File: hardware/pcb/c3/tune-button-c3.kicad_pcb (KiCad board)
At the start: 2 copper layers, 46 x 70 mm, 42 parts, among them J1 USB-C, J2 LiPo, Q1 AO3401A, SW1 MX switch, SW2 MX switch, SW3 MX switch, SW4 MX switch, SW5 RESET, SW6 BOOT, U1 ESP32-C3-WROOM-02-N4, U2 SRV05-4, U3 TP4054, U4 RT9080-3.3

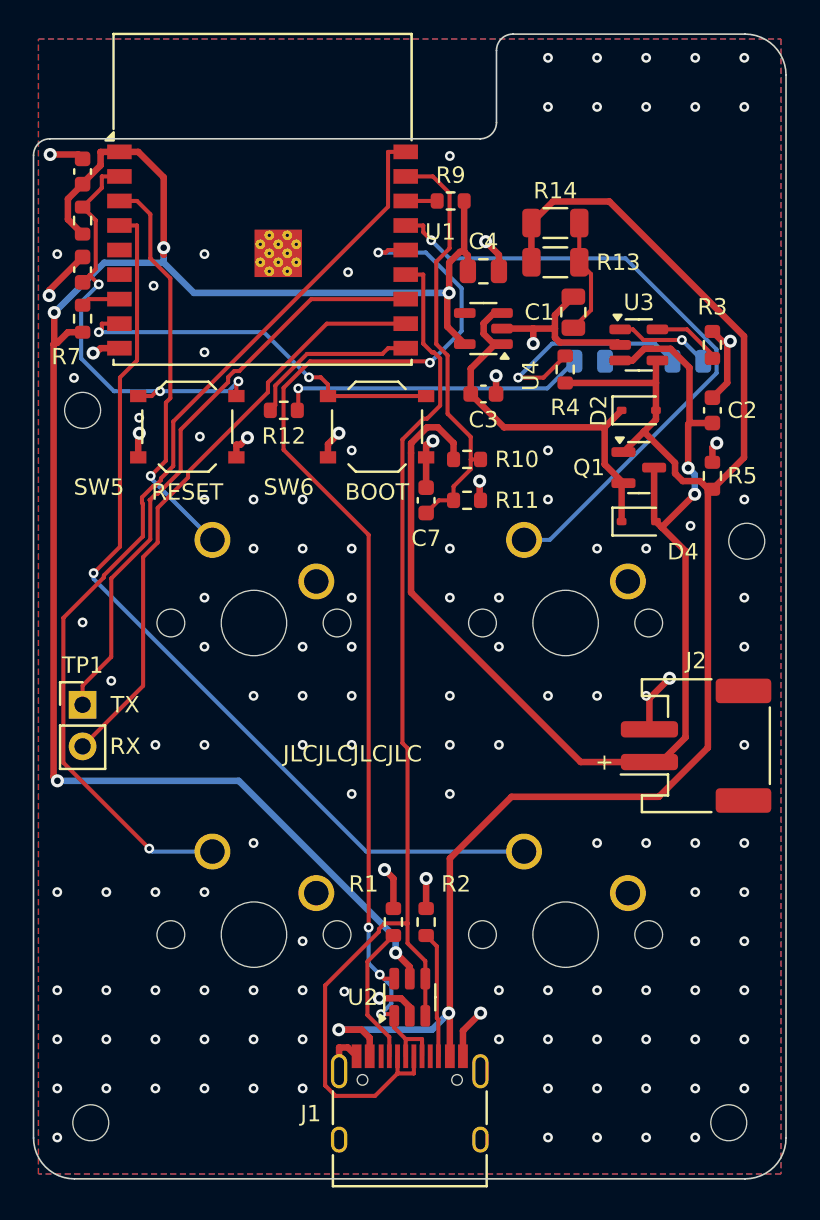
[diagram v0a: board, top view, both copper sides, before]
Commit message: pcb (c3): USB-C at HRO's recommended board edge
HRO's layout puts the board edge 5.79 mm from the receptacle's locating
holes, so its face overhangs by 0.46 mm. It was 6.05 mm (0.2 mm overhang),
which JLC's +-0.2 mm outline tolerance could take to flush, leaving a plug's
moulding nothing to clear the board by. The board is 0.26 mm shorter
(46 x 69.7 mm): the USB-C keeps its place relative to the keys, and what is
placed from the bottom edge (U2, R1, R2, the lower mounting holes) moves up
with it.
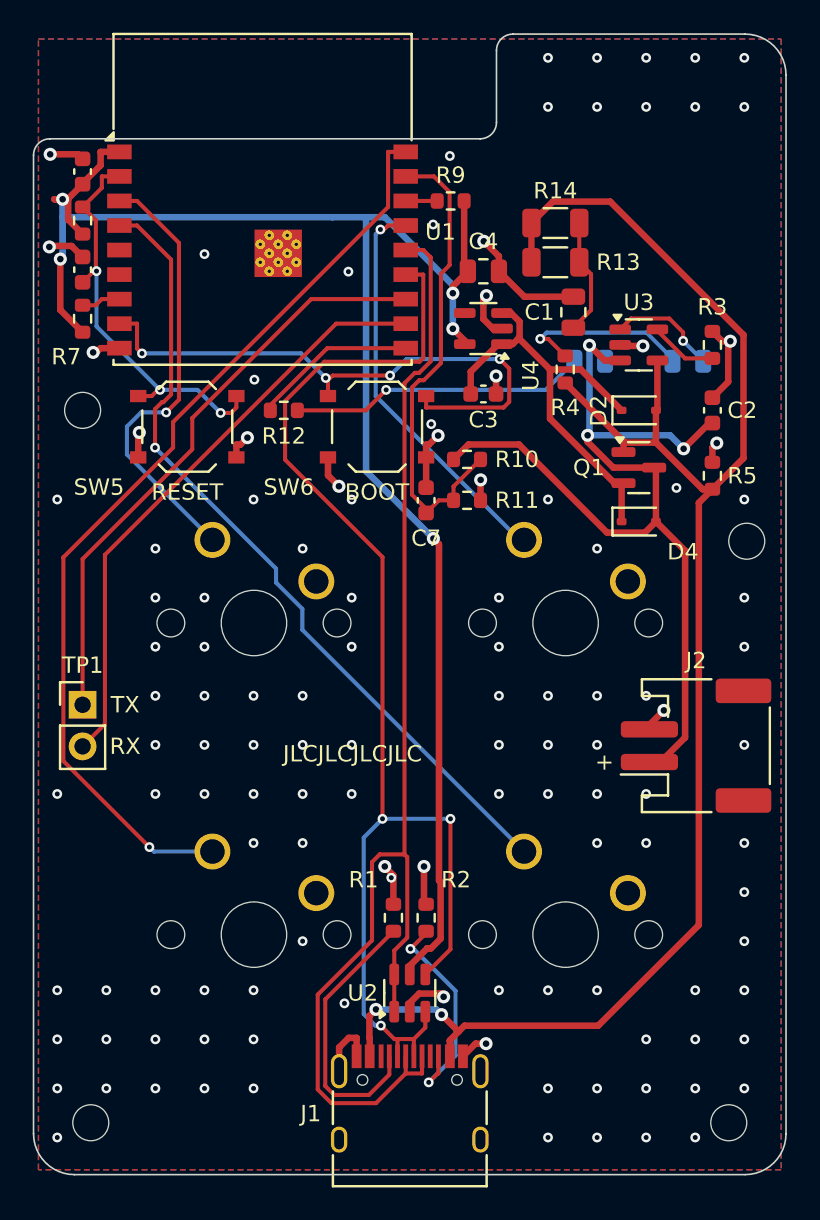
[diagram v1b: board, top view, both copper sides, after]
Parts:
- moved U2 0.26 mm to (23.0, 58.6)
- moved R1 0.26 mm to (22.0, 54.0)
- moved R2 0.26 mm to (24.0, 54.0)
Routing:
- net K1: track 39.8 -> 24.7 mm
- net VBAT: track 69.7 -> 57.2 mm, vias 2 -> 3
- net IO9: track 23.7 -> 35.9 mm, vias 2 -> 4
- net 3V3: track 112.7 -> 102.2 mm
- net USB_DN: track 69.7 -> 78.2 mm, vias 0 -> 3
- net CC1: track 8.59 -> 17.0 mm
- net K3: track 57.0 -> 50.0 mm
- net CC2: track 7.69 -> 13.4 mm, vias 0 -> 2
- net USB_DP: track 70.7 -> 76.1 mm, vias 5 -> 0
- net VSYS: track 23.8 -> 27.1 mm
- net GND: track 54.4 -> 51.1 mm, vias 134 -> 124
- net VBAT_SENSE: track 26.1 -> 29.3 mm
- net CHG_A: track 14.2 -> 11.0 mm
- net VBUS: track 104.5 -> 101.6 mm
- net K2: track 24.7 -> 27.2 mm
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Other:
- board size 46 x 70 mm -> 46 x 69.7 mm

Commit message: pcb: fixes from the sixth DFM audit
- Back-side SMD parts (the hand-soldered LEDs) get a rule area between
  their pads: no tracks, vias or pour there. The re-route had threaded
  VBAT between D3's pads, beside its GND pad, where a solder bridge would
  short the battery.
- Stitching now aims for two GND vias at least 2 mm apart in every pour
  island, not one. U3's ground pad (the charger's heat path) sits on a
  30 mm2 island with three vias; it had been on a 10 mm2 one with one.
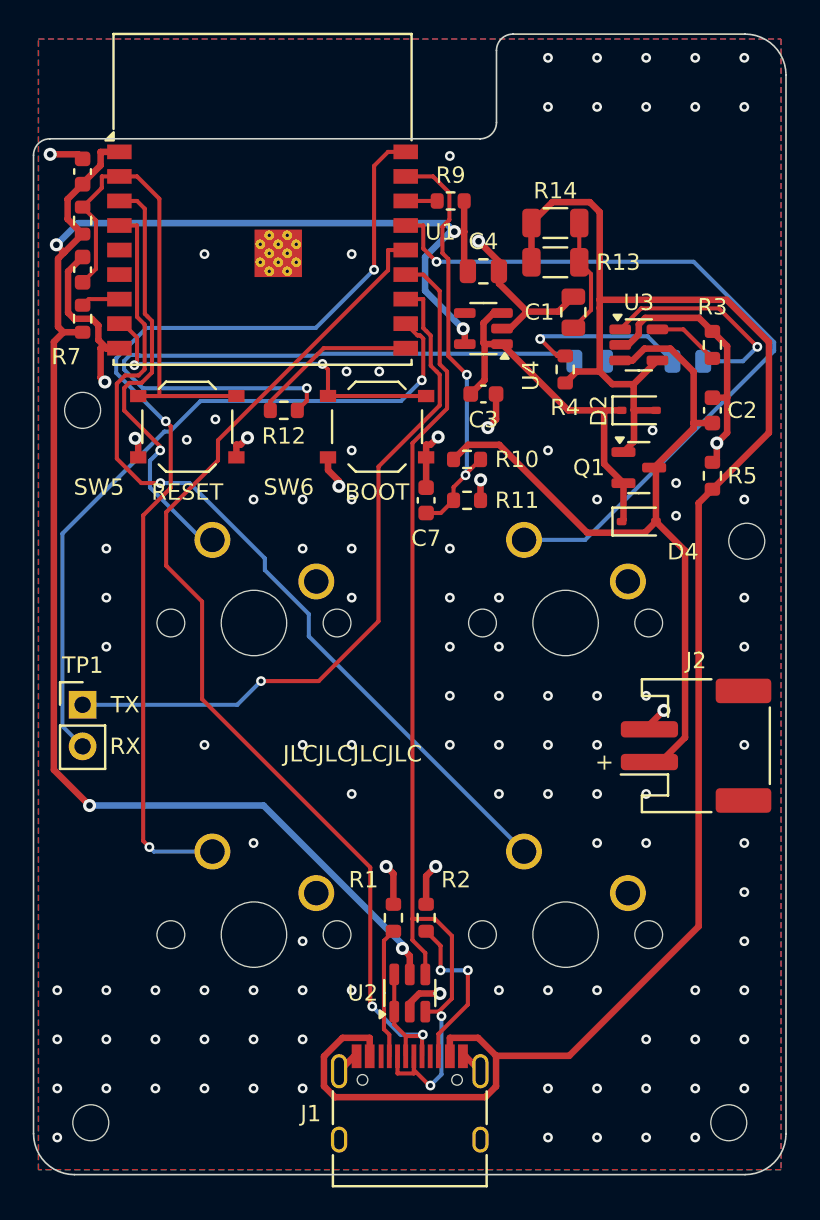
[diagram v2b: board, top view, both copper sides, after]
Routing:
- net LED_A: track 18.2 -> 41.7 mm
- net K1: track 24.7 -> 46.9 mm
- net VBUS: track 101.6 -> 117.9 mm, vias 2 -> 0
- net USB_DN: track 78.2 -> 63.7 mm, vias 3 -> 2
- net GND: track 51.1 -> 65.0 mm, vias 124 -> 116
- net IO9: track 35.9 -> 22.8 mm, vias 4 -> 2
- net CC1: track 17.0 -> 8.01 mm
- net VBAT: track 57.2 -> 48.7 mm, vias 3 -> 0
- net 3V3: track 102.2 -> 109.6 mm
- net RXD: track 36.5 -> 43.4 mm, vias 0 -> 1
- net STAT: track 6.75 -> 13.6 mm
- net TXD: track 36.4 -> 42.9 mm, vias 0 -> 1
- net USB_DP: track 76.1 -> 69.7 mm, vias 0 -> 2
- net K4: track 57.9 -> 62.8 mm, vias 1 -> 3
- net EN: track 25.3 -> 29.8 mm, vias 3 -> 0
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
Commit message: c3: keep tracks out from under the USB-C shell; lay the D+/D- crossover
Round-7 DFM: VBUS ran under J1's grounded shell, insulated only by mask. A
track-free rule area now covers the body from 1.2 mm past the pad tips. With it
the router could no longer join the interleaved D-/D+ pads reliably, so gen.py
lays that crossover itself (D+ across the inner tips, D- through two vias at the
outer tips) and locks it; route.py keeps locked tracks and fails if the session
import drops one.
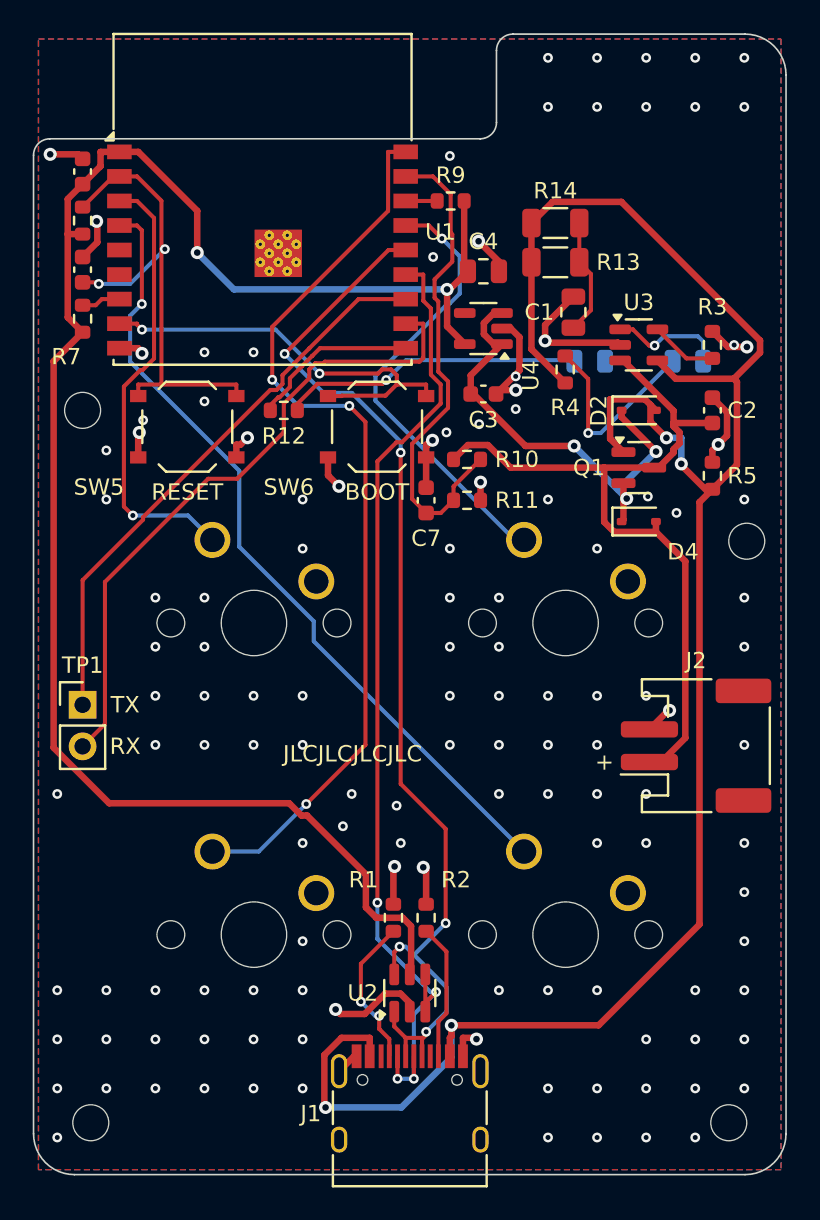
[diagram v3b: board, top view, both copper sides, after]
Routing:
- net LED_A: track 41.7 -> 18.5 mm
- net K1: track 46.9 -> 27.7 mm
- net GND: track 65.0 -> 56.3 mm, vias 116 -> 129
- net TXD: track 42.9 -> 34.9 mm, vias 1 -> 0
- net STAT: track 13.6 -> 7.06 mm
- net K4: track 62.8 -> 56.5 mm
- net VBUS: track 117.9 -> 123.5 mm, vias 0 -> 4
- net VSYS: track 23.5 -> 28.9 mm, vias 0 -> 3
- net 3V3: track 109.6 -> 105.9 mm, vias 5 -> 2
- net VBAT_SENSE: track 26.4 -> 30.0 mm, vias 2 -> 0
- net IO9: track 22.8 -> 26.1 mm
- net RXD: track 43.4 -> 40.3 mm, vias 1 -> 0
- net K3: track 52.8 -> 49.7 mm
- net USB_DP: track 69.7 -> 67.3 mm, vias 2 -> 5
- net CC2: track 10.4 -> 8.36 mm, vias 2 -> 0
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
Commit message: pcb: round-8 audit suggestions
- J1 keepout starts at the shell's metal floor (0.7 mm past the pad tips);
  the D- stubs stop short of it.
- VBUS pad pairs joined through their own power vias and a back-side link,
  so VBUS no longer runs along the GND pads and shell legs.
- D+ link 0.5 mm clear of the A7/B7 tips.
- U2 (ESD) gets its own GND via off its ground pin; U2 moves 0.5 mm up for it.
- Stitcher gives a via-less GND island one wherever a via fits in both pours.
- No vias within 0.6 mm of back-side hand-soldered pads, or under part labels
  and the JLC mark.
- route.py drops zero-length segments with the duplicates.
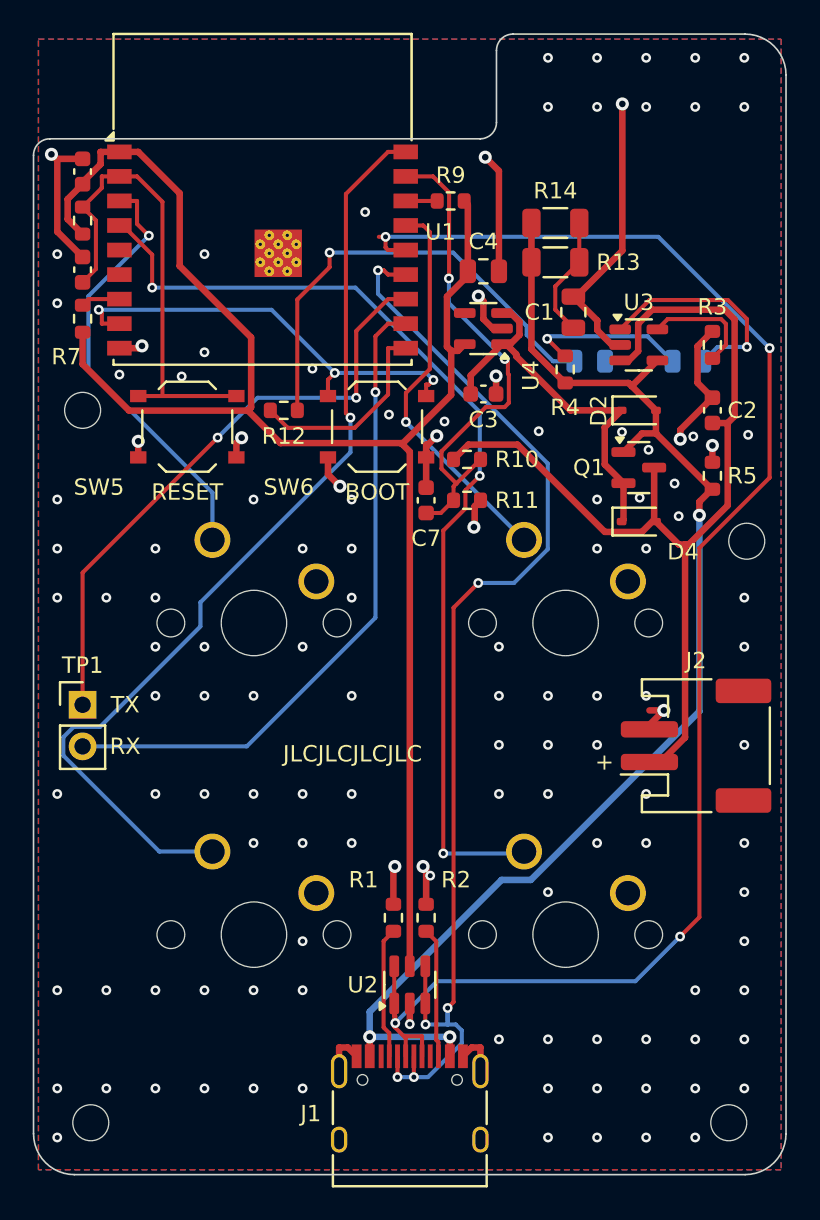
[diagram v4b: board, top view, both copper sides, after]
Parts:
- moved U2 0.50 mm to (23.0, 58.1)
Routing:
- net VBUS: track 123.5 -> 78.3 mm, vias 4 -> 3
- net USB_DP: track 67.3 -> 95.1 mm, vias 5 -> 4
- net GND: track 56.3 -> 73.2 mm, vias 129 -> 127
- net VBAT: track 48.1 -> 61.0 mm
- net K3: track 49.7 -> 60.8 mm, vias 1 -> 3
- net LED_A: track 18.5 -> 28.5 mm
- net USB_DN: track 62.2 -> 71.0 mm, vias 4 -> 6
- net STAT: track 7.06 -> 13.7 mm
- net 3V3: track 105.9 -> 100.8 mm, vias 2 -> 0
- net VSYS: track 28.9 -> 24.0 mm, vias 3 -> 0
- net K1: track 27.7 -> 24.1 mm
- net PROG: track 4.10 -> 7.02 mm
- net K4: track 56.5 -> 58.9 mm, vias 3 -> 1
- net CHG_A: track 12.3 -> 9.89 mm
- net TXD: track 34.9 -> 37.1 mm, vias 0 -> 2
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
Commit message: pcb: round-9 audit fixes; freeze the routing
Round 9 suggestions: keep back tracks off the logo, vias out from under all
front text, standard VBUS vias 0.5 mm out, drop sub-10 um segments, space
stitching vias by copper and anchor islands to any GND via, and reject
autoroute attempts that drop back-plane pour or run another net within
0.4 mm of a switch pin.

Freerouting lays the board out afresh on every run, so each review was of a
new layout. route.py now replays a reviewed routing from <board>/routing.json;
--reroute autoroutes, --freeze records. The back-part via margin is 0.25 mm
(vias are tented; at 0.6 mm the router ran out of room). XIAO: K3 moved off
SW1 pin 1; C3: two stitching vias removed from under the SW3/SW4 labels.
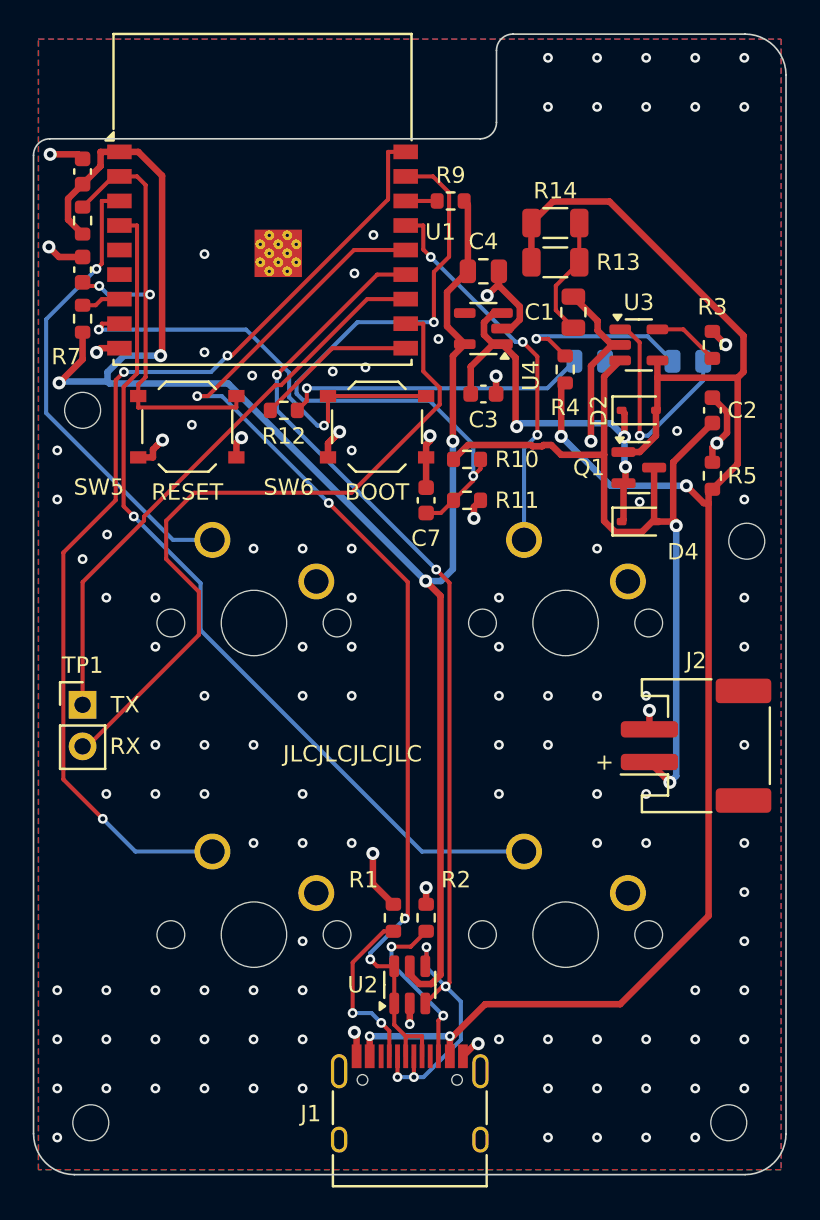
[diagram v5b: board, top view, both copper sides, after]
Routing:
- net VBUS: track 78.3 -> 108.0 mm, vias 3 -> 4
- net USB_DP: track 95.1 -> 67.7 mm
- net GND: track 73.2 -> 51.1 mm, vias 127 -> 125
- net VBAT_SENSE: track 30.3 -> 41.1 mm
- net LED_A: track 28.5 -> 18.6 mm
- net 3V3: track 100.8 -> 110.2 mm, vias 0 -> 4
- net VBAT: track 61.0 -> 53.2 mm, vias 0 -> 2
- net K3: track 60.8 -> 53.5 mm, vias 3 -> 1
- net RXD: track 40.5 -> 43.8 mm, vias 1 -> 0
- net K4: track 58.9 -> 61.9 mm, vias 1 -> 3
- net PROG: track 7.02 -> 4.10 mm
- net CC2: track 7.95 -> 10.6 mm, vias 0 -> 2
- net CC1: track 8.03 -> 10.6 mm, vias 0 -> 2
- net TXD: track 37.1 -> 34.6 mm, vias 2 -> 0
- net VSYS: track 24.0 -> 26.6 mm, vias 0 -> 3
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
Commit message: pcb: round-10 audit fixes
- The pin-gap check covers every hand-soldered through-hole pin (no LCSC
  number): switches on both layers, headers and sockets on the solder side,
  0.4 mm, or 0.29 mm for a track crossing a header row between two pins.
- Replaying routing.json runs the pin-gap and lost-pour checks too, so a
  hand edit has to meet them.
- XIAO: K2 moved 0.4 mm clear of J1 pins 4-7; K4 centred between J2 pins 4
  and 5. C3: K4 moved 0.4 mm clear of TP1.
- C3: second GND vias on the strip beside D+ (R2) and on the R5 island.
- Segments under 0.02 mm are dropped; two such were removed.
- README: nylon washers or standoffs at the C3's mounting holes (H3 has
  tracks within 2 mm).
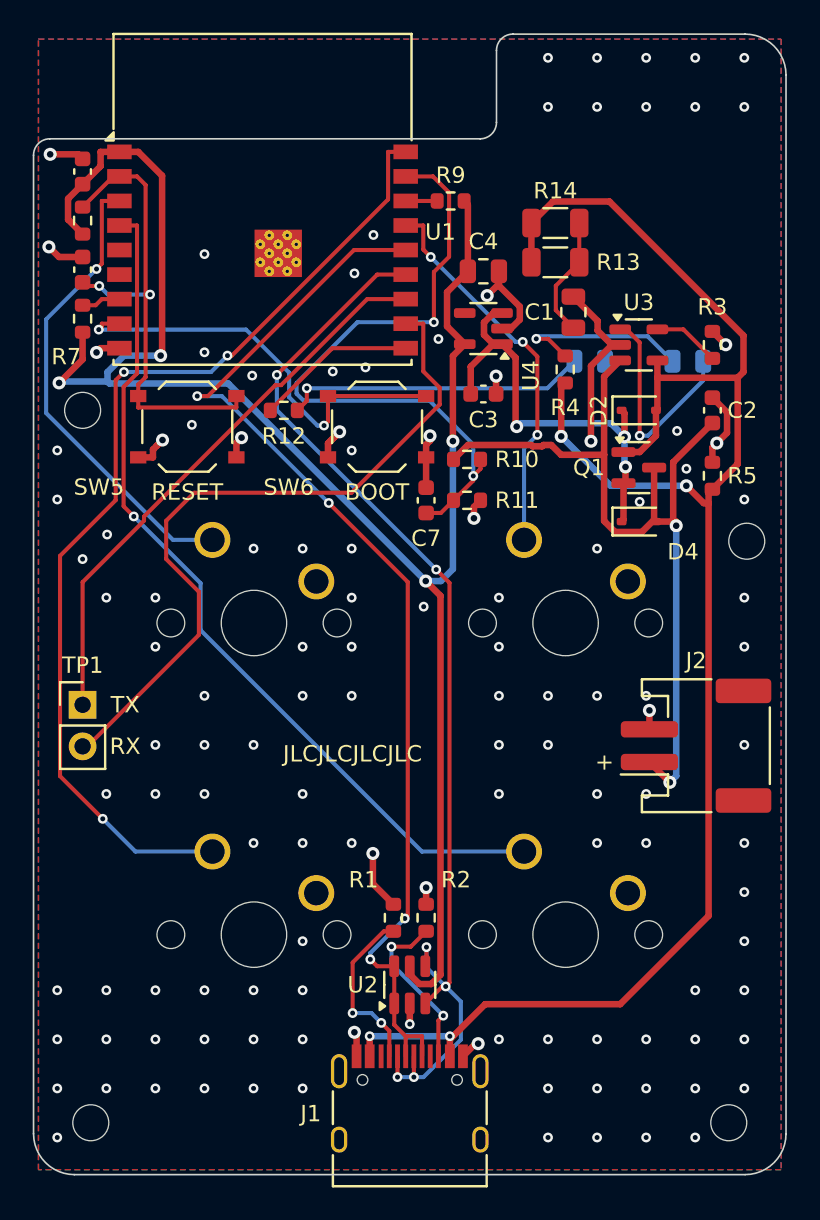
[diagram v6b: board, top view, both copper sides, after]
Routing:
- net GND: vias 125 -> 127
